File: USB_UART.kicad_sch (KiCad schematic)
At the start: 9 parts, among them J1 USB Type C Connector, U4 FT232RL

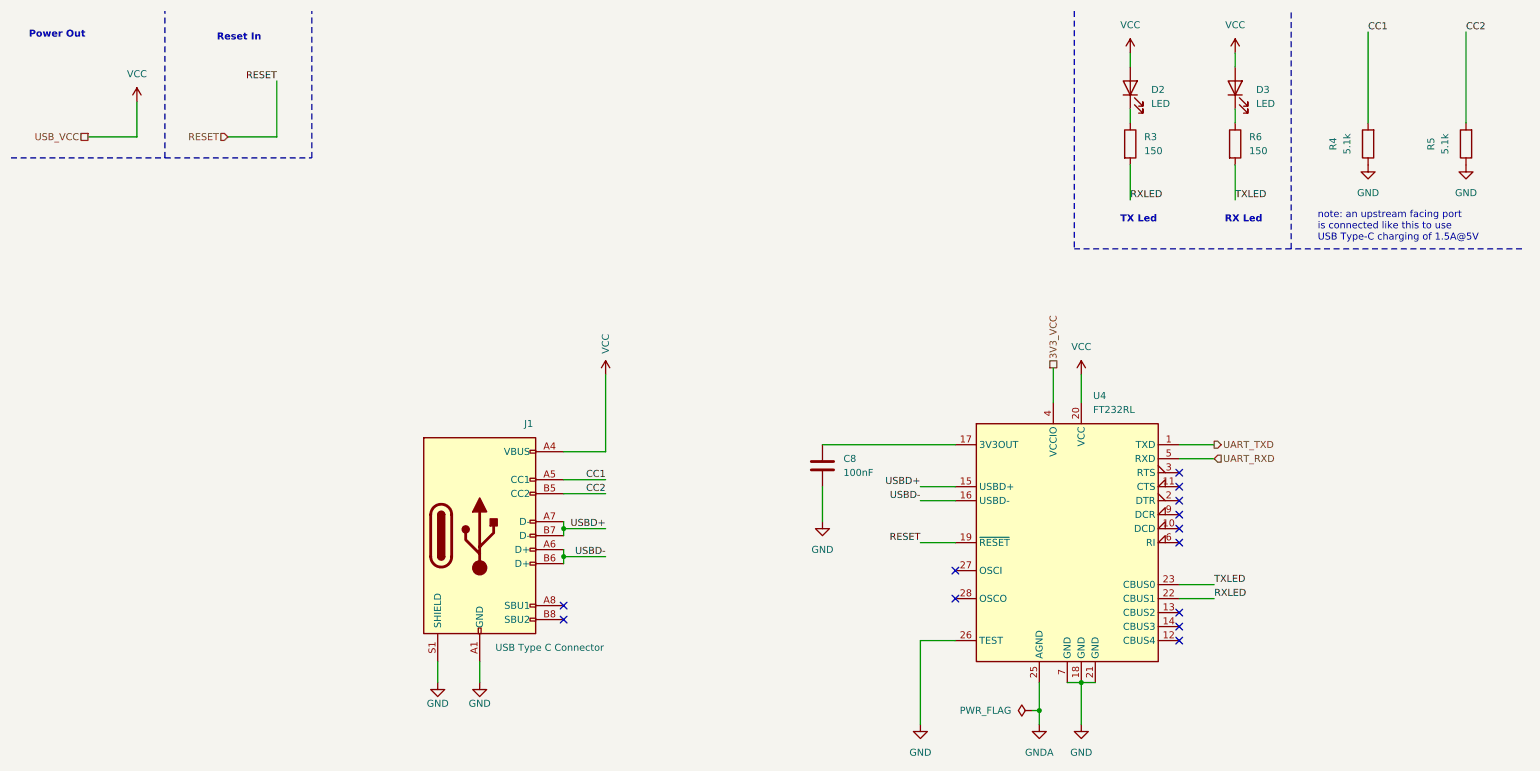
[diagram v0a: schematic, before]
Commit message: feat(usb-uart): add ferrite bead FB2 and replace generic VCC with explicit rails
Adds a Device:Ferrite_Bead (FB2) on the USB VBUS input to filter conducted noise into the board. Replaces the generic power:VCC references in this sheet with explicit power:+5V and power:+3.3V symbols, and drops the USB_VCC and 3V3_VCC hierarchical labels now that the rails are referenced directly via power symbols. R4 retained.
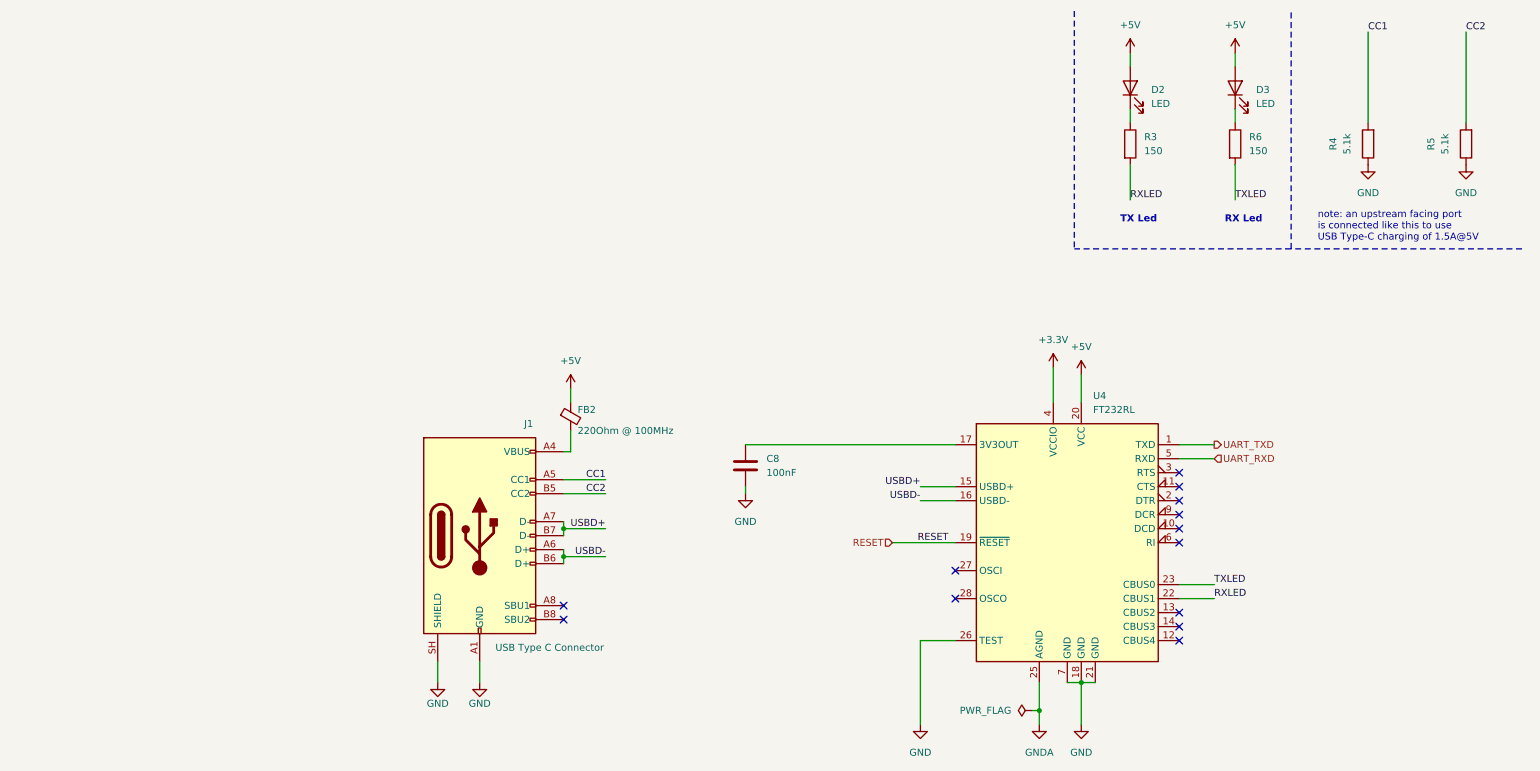
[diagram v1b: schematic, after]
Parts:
- added FB2: 220Ohm @ 100MHz, Inductor_SMD:L_0805_2012Metric_Pad1.05x1.20mm_HandSolder, symbol Device:FerriteBead_Small
- J1: footprint (none) -> Connector_USB:USB_C_Receptacle_GCT_USB4105-xx-A_16P_TopMnt_Horizontal
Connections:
- net GND: now also J1.SH (SHIELD); no longer J1.S1 (SHIELD)
- net 3V3_VCC renamed +3.3V
- net VCC: no longer names the net of J1.A4 (VBUS), J1.A9 (VBUS), J1.B4 (VBUS), J1.B9 (VBUS)
- net VCC: now also FB2.2; no longer D2.2 (A), D3.2 (A), U4.20 (VCC)
- new net +5V: D2.2 (A), D3.2 (A), FB2.1, U4.20 (VCC)
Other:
- note removed: "Power Out"
- note removed: "Reset In"
- moved on the sheet: C8

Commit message: fix(fixed_annotation): sorted by x position
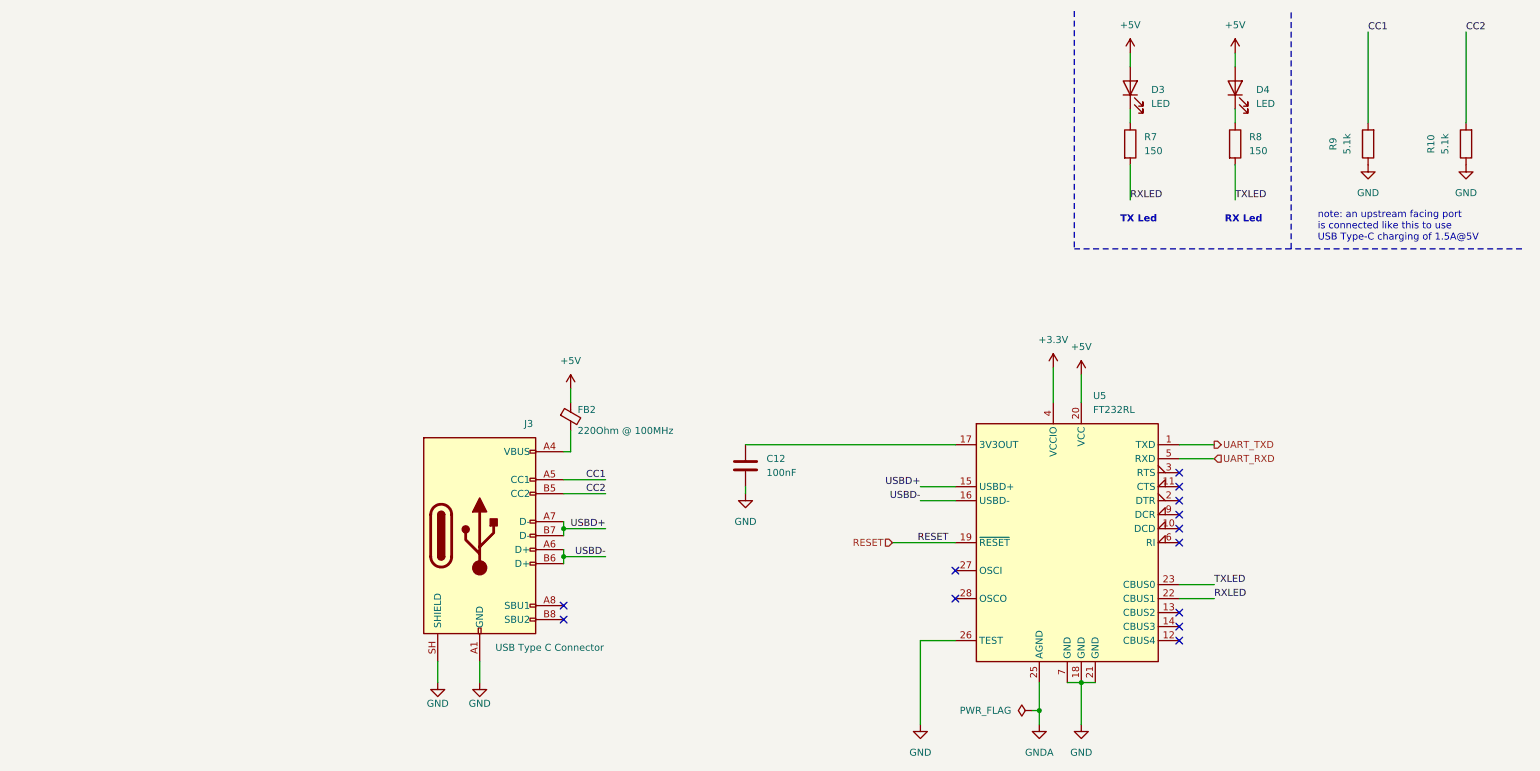
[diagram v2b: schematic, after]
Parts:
- renumbered C8 to C12, D2 to D3, D3 to D4, J1 to J3, R5 to R10, R3 to R7, R6 to R8, R4 to R9, U4 to U5
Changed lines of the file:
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@@
 		(dnp no)
 		(fields_autoplaced yes)
-		(property "Reference" "#FLG02"
+		(property "Reference" "#FLG05"
 			(at 193.675 139.7 0)
 			(hide yes)
@@
 			(project "HW"
 				(path "/01550cd7-b424-469c-925b-c370f3609cd4/b4895c98-2d65-46cb-a7d2-9672cea4def2"
-					(reference "#FLG02")
+					(reference "#FLG05")
 					(unit 1)
 				)
@@
 		(dnp no)
 		(fields_autoplaced yes)
-		(property "Reference" "#PWR035"
+		(property "Reference" "#PWR058"
 			(at 274.32 46.99 0)
 			(hide yes)
@@
 			(project "HW"
 				(path "/01550cd7-b424-469c-925b-c370f3609cd4/b4895c98-2d65-46cb-a7d2-9672cea4def2"
-					(reference "#PWR035")
+					(reference "#PWR058")
 					(unit 1)
 				)
@@
 		(in_pos_files yes)
 		(dnp no)
-		(property "Reference" "R5"
+		(property "Reference" "R10"
 			(at 267.97 36.83 90)
 			(show_name no)
@@
 			(project "HW"
 				(path "/01550cd7-b424-469c-925b-c370f3609cd4/b4895c98-2d65-46cb-a7d2-9672cea4def2"
-					(reference "R5")
+					(reference "R10")
 					(unit 1)
 				)
@@
 		(dnp no)
 		(fields_autoplaced yes)
-		(property "Reference" "U4"
+		(property "Reference" "U5"
 			(at 206.6133 82.55 0)
 			(show_name no)
@@
 			(project "HW"
 				(path "/01550cd7-b424-469c-925b-c370f3609cd4/b4895c98-2d65-46cb-a7d2-9672cea4def2"
-					(reference "U4")
+					(reference "U5")
 					(unit 1)
 				)
@@
 		(dnp no)
 		(fields_autoplaced yes)
-		(property "Reference" "#PWR032"
+		(property "Reference" "#PWR050"
 			(at 175.26 148.59 0)
 			(hide yes)
@@
 			(project "HW"
 				(path "/01550cd7-b424-469c-925b-c370f3609cd4/b4895c98-2d65-46cb-a7d2-9672cea4def2"
-					(reference "#PWR032")
+					(reference "#PWR050")
 					(unit 1)
 				)
@@
 		(dnp no)
 		(fields_autoplaced yes)
-		(property "Reference" "#PWR030"
+		(property "Reference" "#PWR056"
 			(at 232.41 24.13 0)
 			(hide yes)
@@
 			(project "HW"
 				(path "/01550cd7-b424-469c-925b-c370f3609cd4/b4895c98-2d65-46cb-a7d2-9672cea4def2"
-					(reference "#PWR030")
+					(reference "#PWR056")
 					(unit 1)
 				)
@@
 		(dnp no)
 		(fields_autoplaced yes)
-		(property "Reference" "D3"
+		(property "Reference" "D4"
 			(at 236.22 26.9874 90)
 			(show_name no)
@@
 			(project "HW"
 				(path "/01550cd7-b424-469c-925b-c370f3609cd4/b4895c98-2d65-46cb-a7d2-9672cea4def2"
-					(reference "D3")
+					(reference "D4")
 					(unit 1)
 				)
@@
 		(in_pos_files yes)
 		(dnp no)
-		(property "Reference" "R4"
+		(property "Reference" "R9"
 			(at 250.19 36.83 90)
 			(show_name no)
@@
 			(project "HW"
 				(path "/01550cd7-b424-469c-925b-c370f3609cd4/b4895c98-2d65-46cb-a7d2-9672cea4def2"
-					(reference "R4")
+					(reference "R9")
 					(unit 1)
 				)
@@
 		(dnp no)
 		(fields_autoplaced yes)
-		(property "Reference" "#PWR029"
+		(property "Reference" "#PWR055"
 			(at 213.36 24.13 0)
 			(hide yes)
@@
 			(project "HW"
 				(path "/01550cd7-b424-469c-925b-c370f3609cd4/b4895c98-2d65-46cb-a7d2-9672cea4def2"
-					(reference "#PWR029")
+					(reference "#PWR055")
 					(unit 1)
 				)
@@
 		(dnp no)
 		(fields_autoplaced yes)
-		(property "Reference" "#PWR034"
+		(property "Reference" "#PWR057"
 			(at 256.54 46.99 0)
 			(hide yes)
@@
 			(project "HW"
 				(path "/01550cd7-b424-469c-925b-c370f3609cd4/b4895c98-2d65-46cb-a7d2-9672cea4def2"
-					(reference "#PWR034")
+					(reference "#PWR057")
 					(unit 1)
 				)
@@
 		(in_pos_files yes)
 		(dnp no)
-		(property "Reference" "#PWR017"
+		(property "Reference" "#PWR047"
 			(at 95.25 140.97 0)
 			(hide yes)
@@
 			(project "HW"
 				(path "/01550cd7-b424-469c-925b-c370f3609cd4/b4895c98-2d65-46cb-a7d2-9672cea4def2"
-					(reference "#PWR017")
+					(reference "#PWR047")
 					(unit 1)
 				)
@@
 		(dnp no)
 		(fields_autoplaced yes)
-		(property "Reference" "#PWR026"
+		(property "Reference" "#PWR048"
 			(at 111.76 85.09 0)
 			(hide yes)
@@
 			(project "HW"
 				(path "/01550cd7-b424-469c-925b-c370f3609cd4/b4895c98-2d65-46cb-a7d2-9672cea4def2"
-					(reference "#PWR026")
+					(reference "#PWR048")
 					(unit 1)
 				)
@@
 		(dnp no)
 		(fields_autoplaced yes)
-		(property "Reference" "#PWR025"
+		(property "Reference" "#PWR049"
 			(at 143.51 106.68 0)
 			(hide yes)
@@
 			(project "HW"
 				(path "/01550cd7-b424-469c-925b-c370f3609cd4/b4895c98-2d65-46cb-a7d2-9672cea4def2"
-					(reference "#PWR025")
+					(reference "#PWR049")
 					(unit 1)
 				)
@@
 		(dnp no)
 		(fields_autoplaced yes)
-		(property "Reference" "R3"
+		(property "Reference" "R7"
 			(at 215.9 35.5599 0)
 			(show_name no)
@@
 			(project "HW"
 				(path "/01550cd7-b424-469c-925b-c370f3609cd4/b4895c98-2d65-46cb-a7d2-9672cea4def2"
-					(reference "R3")
+					(reference "R7")
 					(unit 1)
 				)
@@
 		(dnp no)
 		(fields_autoplaced yes)
-		(property "Reference" "R6"
+		(property "Reference" "R8"
 			(at 234.95 35.5599 0)
 			(show_name no)
@@
 			(project "HW"
 				(path "/01550cd7-b424-469c-925b-c370f3609cd4/b4895c98-2d65-46cb-a7d2-9672cea4def2"
-					(reference "R6")
+					(reference "R8")
 					(unit 1)
 				)
@@
 		(dnp no)
 		(fields_autoplaced yes)
-		(property "Reference" "D2"
+		(property "Reference" "D3"
 			(at 217.17 26.9874 90)
 			(show_name no)
@@
 			(project "HW"
 				(path "/01550cd7-b424-469c-925b-c370f3609cd4/b4895c98-2d65-46cb-a7d2-9672cea4def2"
-					(reference "D2")
+					(reference "D3")
 					(unit 1)
 				)
@@
 		(dnp no)
 		(fields_autoplaced yes)
-		(property "Reference" "#PWR028"
+		(property "Reference" "#PWR053"
 			(at 204.47 82.55 0)
 			(hide yes)
@@
 			(project "HW"
 				(path "/01550cd7-b424-469c-925b-c370f3609cd4/b4895c98-2d65-46cb-a7d2-9672cea4def2"
-					(reference "#PWR028")
+					(reference "#PWR053")
 					(unit 1)
 				)
@@
 		(in_pos_files yes)
 		(dnp no)
-		(property "Reference" "#PWR018"
+		(property "Reference" "#PWR046"
 			(at 87.63 140.97 0)
 			(hide yes)
@@
 			(project "HW"
 				(path "/01550cd7-b424-469c-925b-c370f3609cd4/b4895c98-2d65-46cb-a7d2-9672cea4def2"
-					(reference "#PWR018")
+					(reference "#PWR046")
 					(unit 1)
 				)
@@
 		(dnp no)
 		(fields_autoplaced yes)
-		(property "Reference" "C8"
+		(property "Reference" "C12"
 			(at 147.32 93.9799 0)
 			(show_name no)
@@
 			(project "HW"
 				(path "/01550cd7-b424-469c-925b-c370f3609cd4/b4895c98-2d65-46cb-a7d2-9672cea4def2"
-					(reference "C8")
+					(reference "C12")
 					(unit 1)
 				)
@@
 		(in_pos_files yes)
 		(dnp no)
-		(property "Reference" "J1"
+		(property "Reference" "J3"
 			(at 104.14 87.63 0)
 			(show_name no)
@@
 			(project "HW"
 				(path "/01550cd7-b424-469c-925b-c370f3609cd4/b4895c98-2d65-46cb-a7d2-9672cea4def2"
-					(reference "J1")
+					(reference "J3")
 					(unit 1)
 				)
@@
 		(dnp no)
 		(fields_autoplaced yes)
-		(property "Reference" "#PWR031"
+		(property "Reference" "#PWR054"
 			(at 204.47 148.59 0)
 			(hide yes)
@@
 			(project "HW"
 				(path "/01550cd7-b424-469c-925b-c370f3609cd4/b4895c98-2d65-46cb-a7d2-9672cea4def2"
-					(reference "#PWR031")
+					(reference "#PWR054")
 					(unit 1)
 				)
@@
 		(dnp no)
 		(fields_autoplaced yes)
-		(property "Reference" "#PWR022"
+		(property "Reference" "#PWR052"
 			(at 199.39 81.28 0)
 			(hide yes)
@@
 			(project "HW"
 				(path "/01550cd7-b424-469c-925b-c370f3609cd4/b4895c98-2d65-46cb-a7d2-9672cea4def2"
-					(reference "#PWR022")
+					(reference "#PWR052")
 					(unit 1)
 				)
@@
 		(dnp no)
 		(fields_autoplaced yes)
-		(property "Reference" "#PWR033"
+		(property "Reference" "#PWR051"
 			(at 196.85 148.59 0)
 			(hide yes)
@@
 			(project "HW"
 				(path "/01550cd7-b424-469c-925b-c370f3609cd4/b4895c98-2d65-46cb-a7d2-9672cea4def2"
-					(reference "#PWR033")
-					(unit 1)
-				)
+					(reference "#PWR051")
+					(unit 1)
+				)
